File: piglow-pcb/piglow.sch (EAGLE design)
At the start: 30 parts, among them IC1 ic-sm3218-qfn24, P1 led-pink-0805, P2 led-pink-0805, P3 led-pink-0805, Y1 led-yellow-0805, Y2 led-yellow-0805, Y3 led-yellow-0805

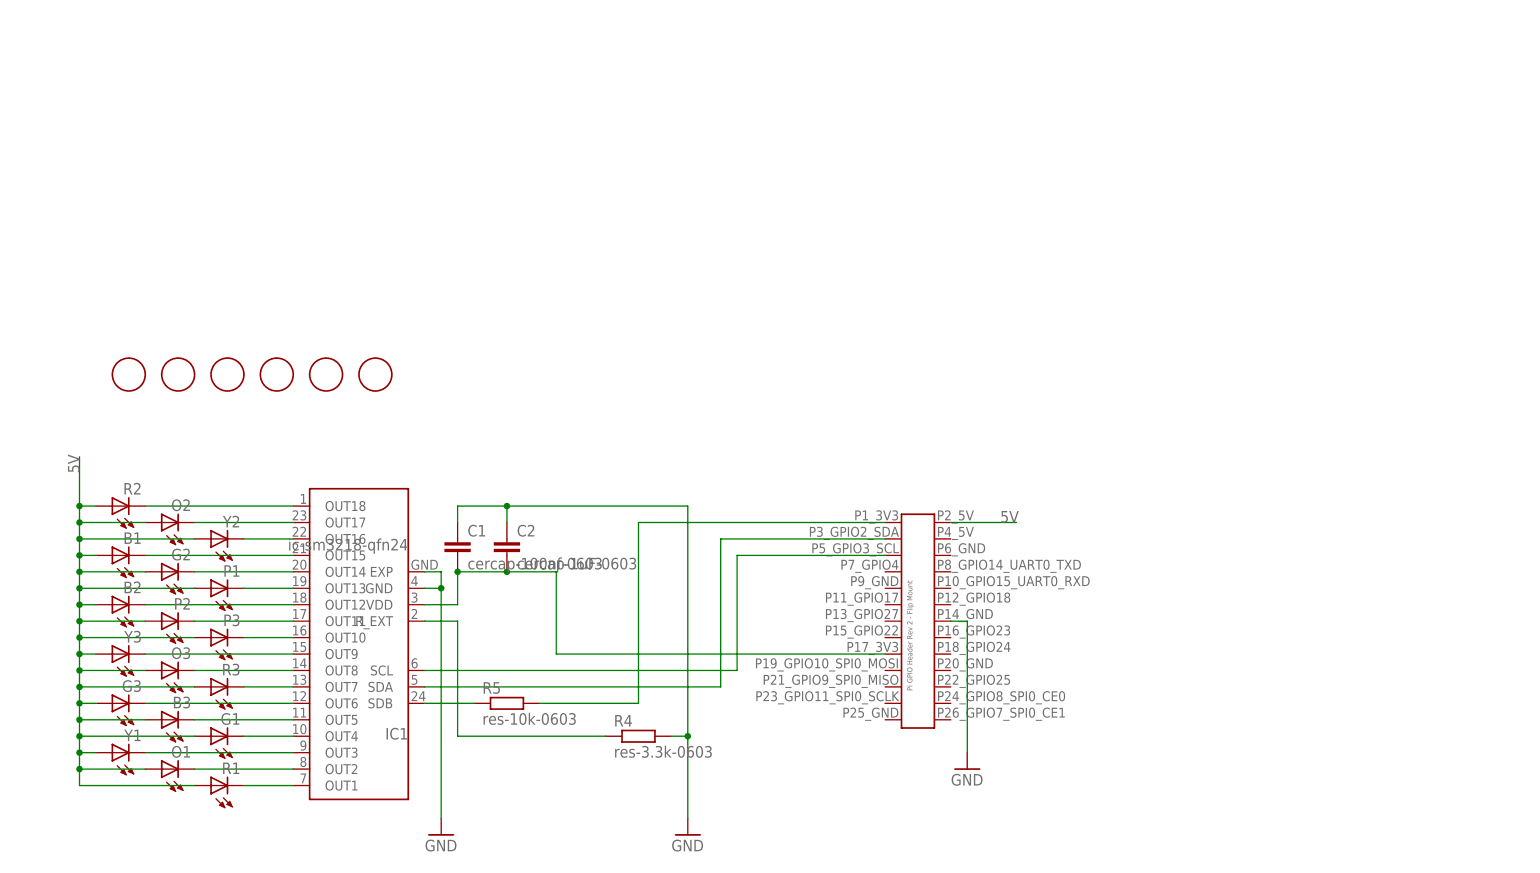
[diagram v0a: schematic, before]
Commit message: Updated SN3218 to new landings
Also Tidied up Schematic and rerouted board with 10mil traces and 8mil
clearance
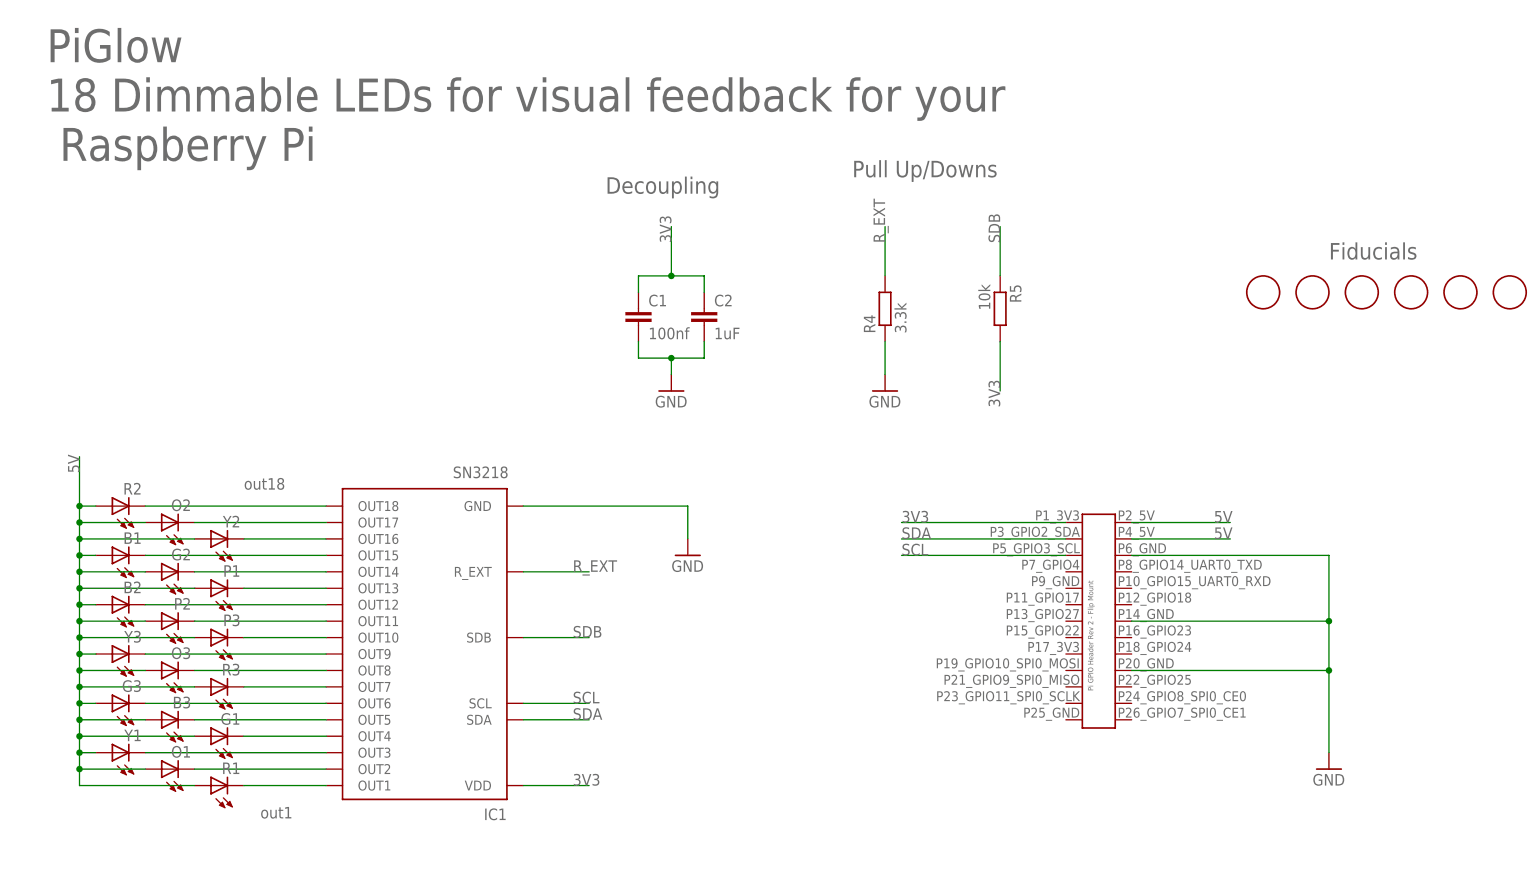
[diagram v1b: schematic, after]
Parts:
- C1: value cercap-100nf-0603 -> 100nf
- C2: value cercap-1uF-0603 -> 1uF
- IC1: value ic-sm3218-qfn24 -> SN3218
- R4: value res-3.3k-0603 -> 3.3k
- R5: value res-10k-0603 -> 10k
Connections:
- net N$1 renamed SCL
- net N$2 renamed SDA
- net N$3 renamed SDB
- removed net N$19: IC1.R_EXT, R4.1
- removed net N$23: C1.2, C2.2, IC1.VDD, U$4.P17_3V3
- removed net VCC: R5.2, U$4.P1_3V3
- new net 3V3: C1.1, C2.1, IC1.VDD, R5.2, U$4.P1_3V3
- new net R_EXT: IC1.R_EXT, R4.2
- net 5V: now also U$4.P4_5V
- net GND: now also C1.2, C2.2, R4.1, U$4.P20_GND, U$4.P6_GND; no longer C1.1, C2.1, IC1.EXP, R4.2
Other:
- note added: "Decoupling"
- note added: "Fiducials"
- note added: "PiGlow 18 Dimmable LEDs for visual feedback for your Raspberry Pi"
- note added: "Pull Up/Downs"
- note added: "out1"
- note added: "out18"
- moved on the sheet: C1, C2, R4, R5

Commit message: Revert "Updated SN3218 to new landings"
This reverts commit 9275a731dc1cb28da2cd379615e04127a905d690.
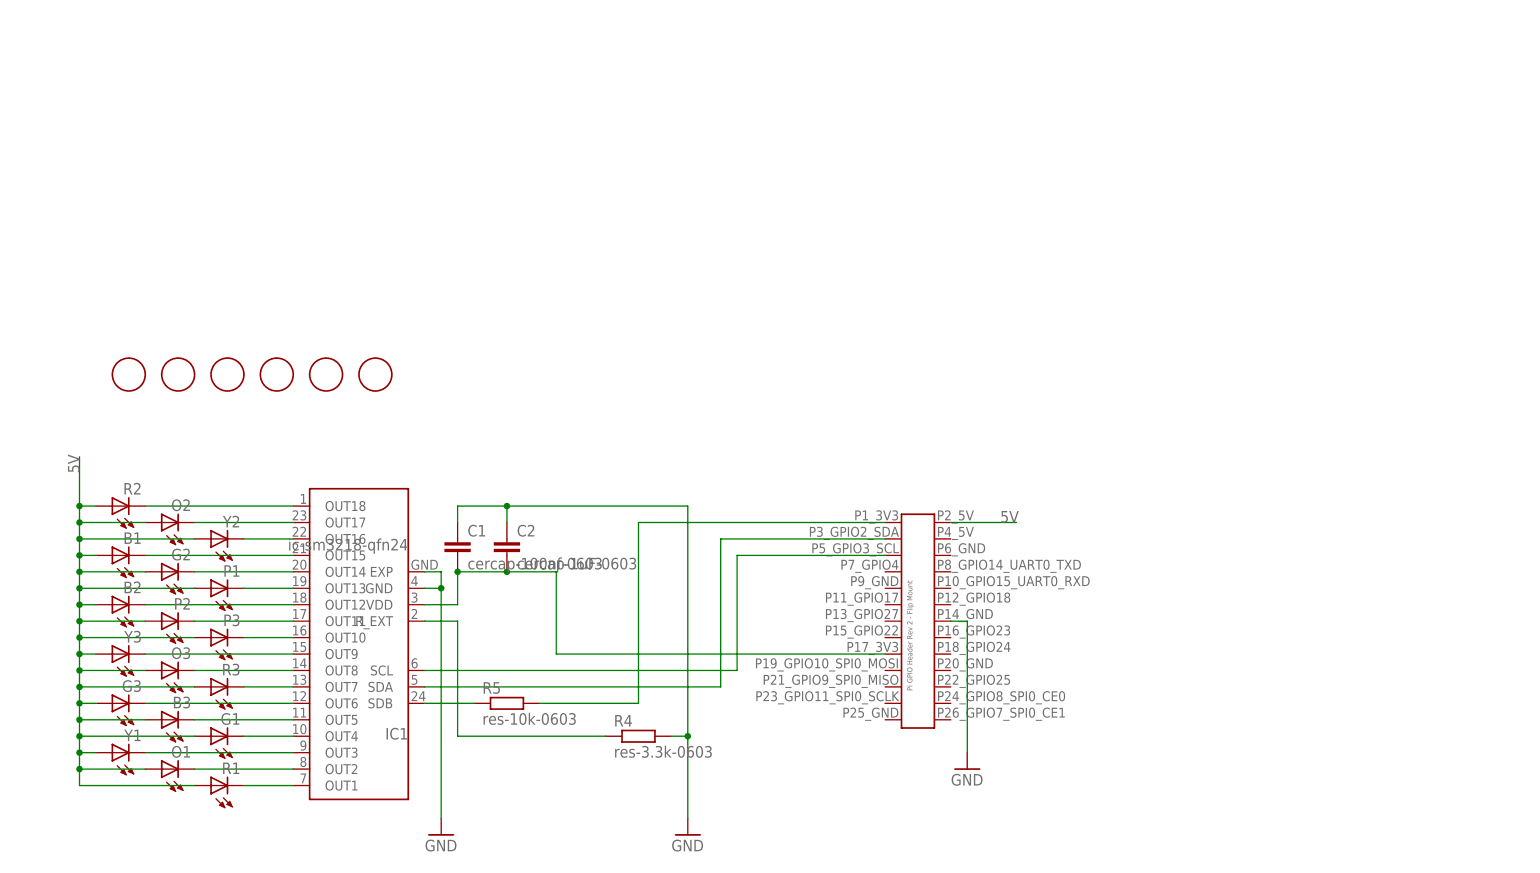
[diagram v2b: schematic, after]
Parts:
- C1: value 100nf -> cercap-100nf-0603
- C2: value 1uF -> cercap-1uF-0603
- IC1: value SN3218 -> ic-sm3218-qfn24
- R4: value 3.3k -> res-3.3k-0603
- R5: value 10k -> res-10k-0603
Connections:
- net SCL renamed N$1
- net SDA renamed N$2
- net SDB renamed N$3
- removed net 3V3: C1.1, C2.1, IC1.VDD, R5.2, U$4.P1_3V3
- removed net R_EXT: IC1.R_EXT, R4.2
- new net N$19: IC1.R_EXT, R4.1
- new net N$23: C1.2, C2.2, IC1.VDD, U$4.P17_3V3
- new net VCC: R5.2, U$4.P1_3V3
- net 5V: no longer U$4.P4_5V
- net GND: now also C1.1, C2.1, IC1.EXP, R4.2; no longer C1.2, C2.2, R4.1, U$4.P20_GND, U$4.P6_GND
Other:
- note removed: "Decoupling"
- note removed: "Fiducials"
- note removed: "PiGlow 18 Dimmable LEDs for visual feedback for your Raspberry Pi"
- note removed: "Pull Up/Downs"
- note removed: "out1"
- note removed: "out18"
- moved on the sheet: C1, C2, R4, R5

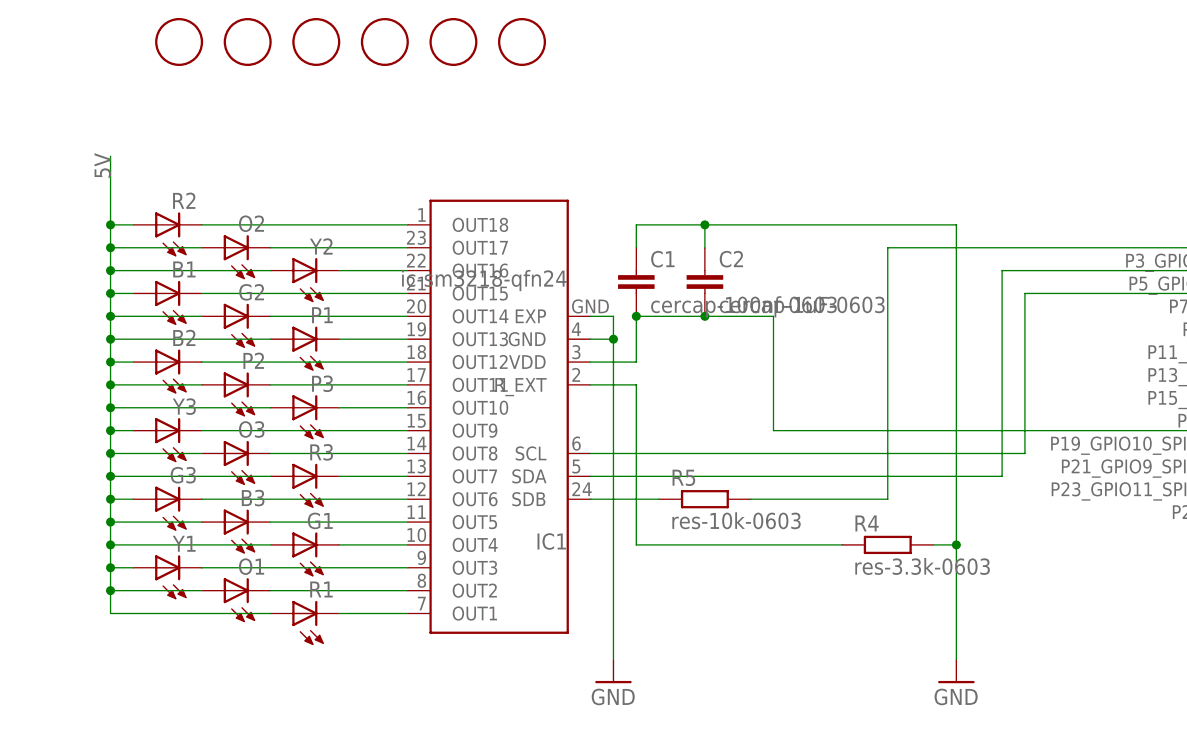
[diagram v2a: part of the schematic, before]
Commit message: New SN3218 landing
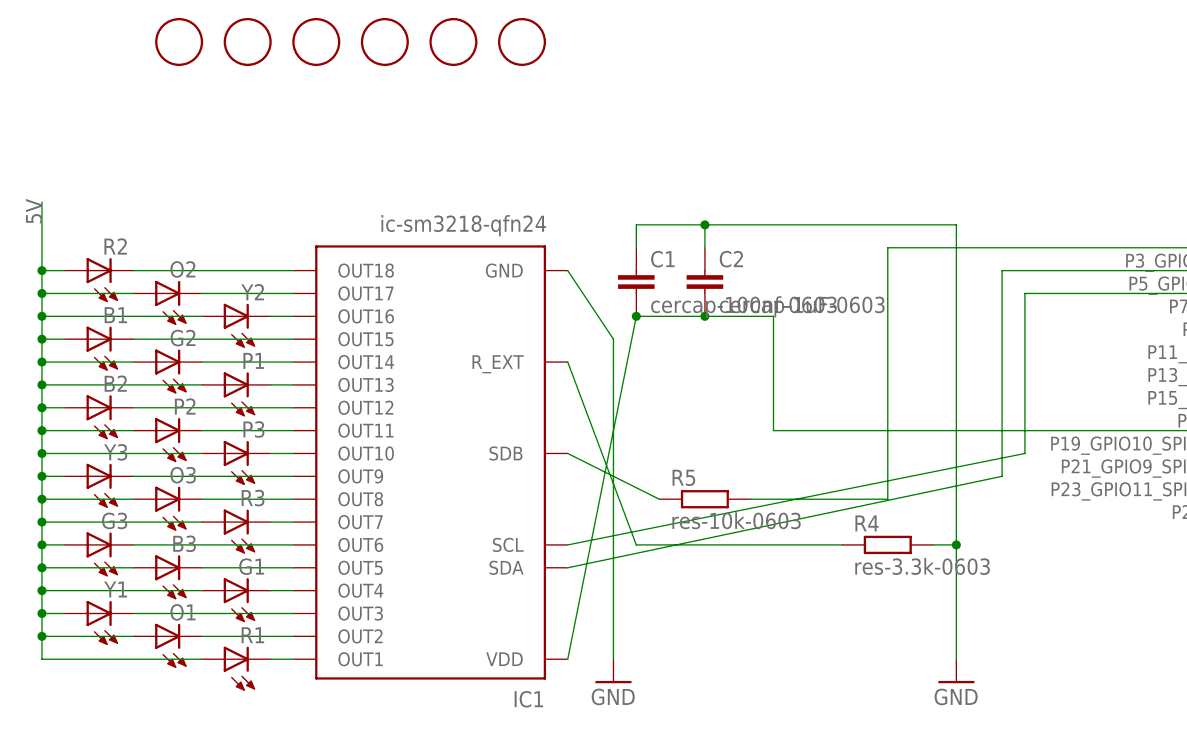
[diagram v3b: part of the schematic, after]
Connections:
- net GND: no longer IC1.EXP
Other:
- moved on the sheet: B1, B2, B3, G1, G2, G3, O1, O2, O3, P1, P2, P3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
